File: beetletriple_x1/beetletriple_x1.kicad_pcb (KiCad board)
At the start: 4 copper layers, 82 x 56.5 mm, 70 parts, among them J1 Power IN, J10 soicbite programming connector, J2 motor_out, J3 motor_out, J4 motor_out, J5 input_c1, J6 input_c2, J7 input_c3, J8 output_c4, J9 output_c5, Q1 IRF8313PBF, Q2 IRF8313PBF, Q3 IRF8313PBF, Q4 IRF8313PBF, Q5 IRF8313PBF, Q6 IRF8313PBF, U1 TPS54331DR, U11 NCP81155MN, U12 NCP81155MN, U13 NCP81155MN, U14 NCP81155MN, U15 NCP81155MN, U16 NCP81155MN, U2 HT7550-1, U3 ATtiny1617-M, U4 78L12G-AB3-R

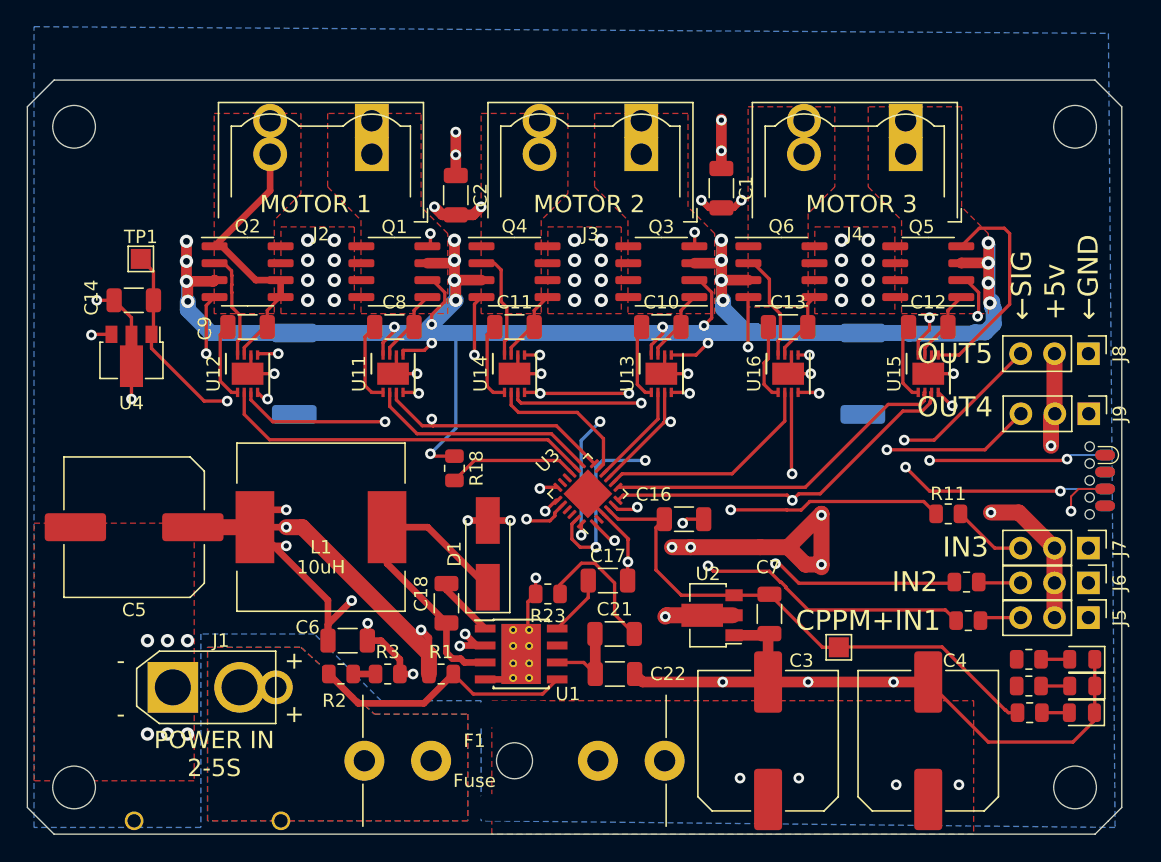
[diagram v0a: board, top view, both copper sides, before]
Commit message: Beetletriple version x1 with the dfn-8 gate driver finally fix up routing and errors
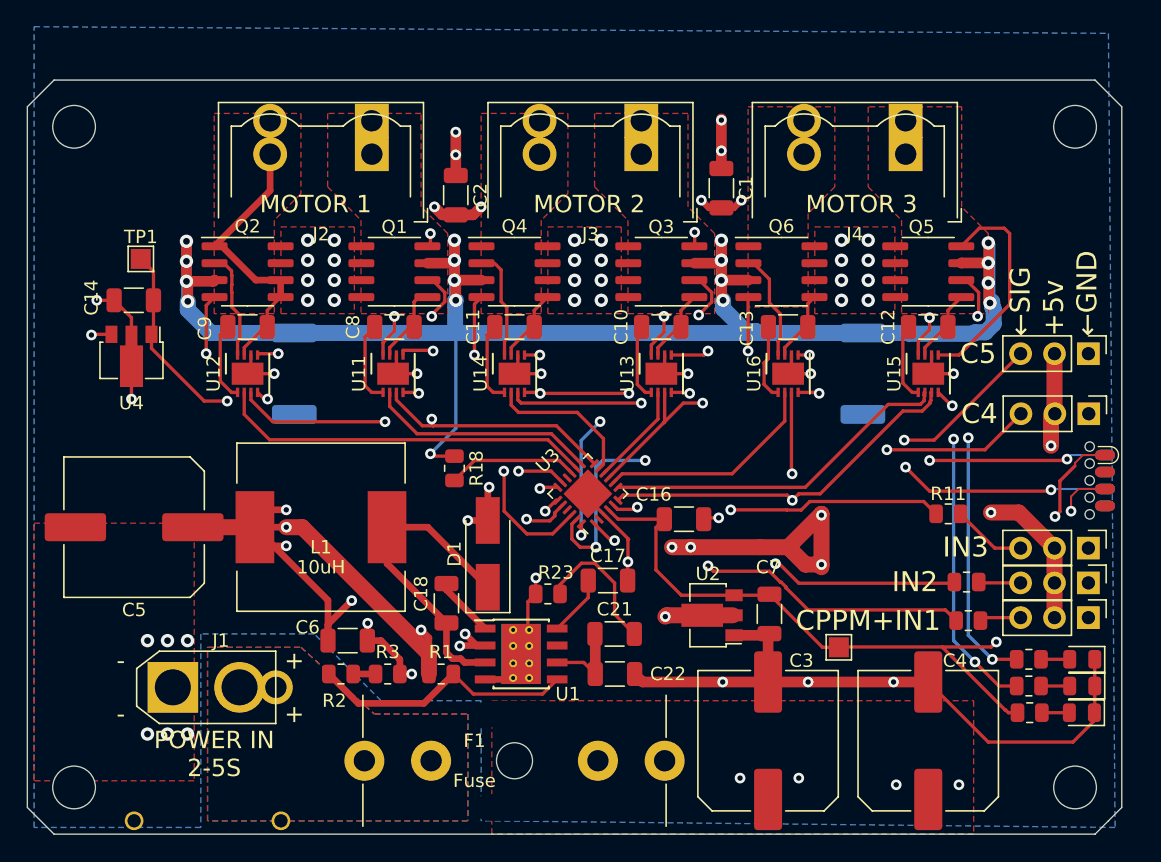
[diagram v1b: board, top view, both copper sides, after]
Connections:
- U3 pad 17: unconnected-(U3-Pad17) -> /MCU/BLINKY2
- U3 pad 21: /MCU/BLINKY2 -> unconnected-(U3-Pad21)
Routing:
- net /MCU/BLINKY1: track 0.00 -> 66.4 mm, vias 0 -> 3
- net /MCU/BLINKY2: track 0.00 -> 60.5 mm, vias 0 -> 3
- net VLOGIC: track 40.7 -> 64.4 mm, vias 0 -> 2
- net MOTOR2EN: track 21.4 -> 26.2 mm
- net /Drivers/GNDSHUNT: track 145.9 -> 144.9 mm
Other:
- board text added: "C4"
- board text added: "C5"
- board text removed: "OUT4"
- board text removed: "OUT5"

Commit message: Add gate resistors; re-layout
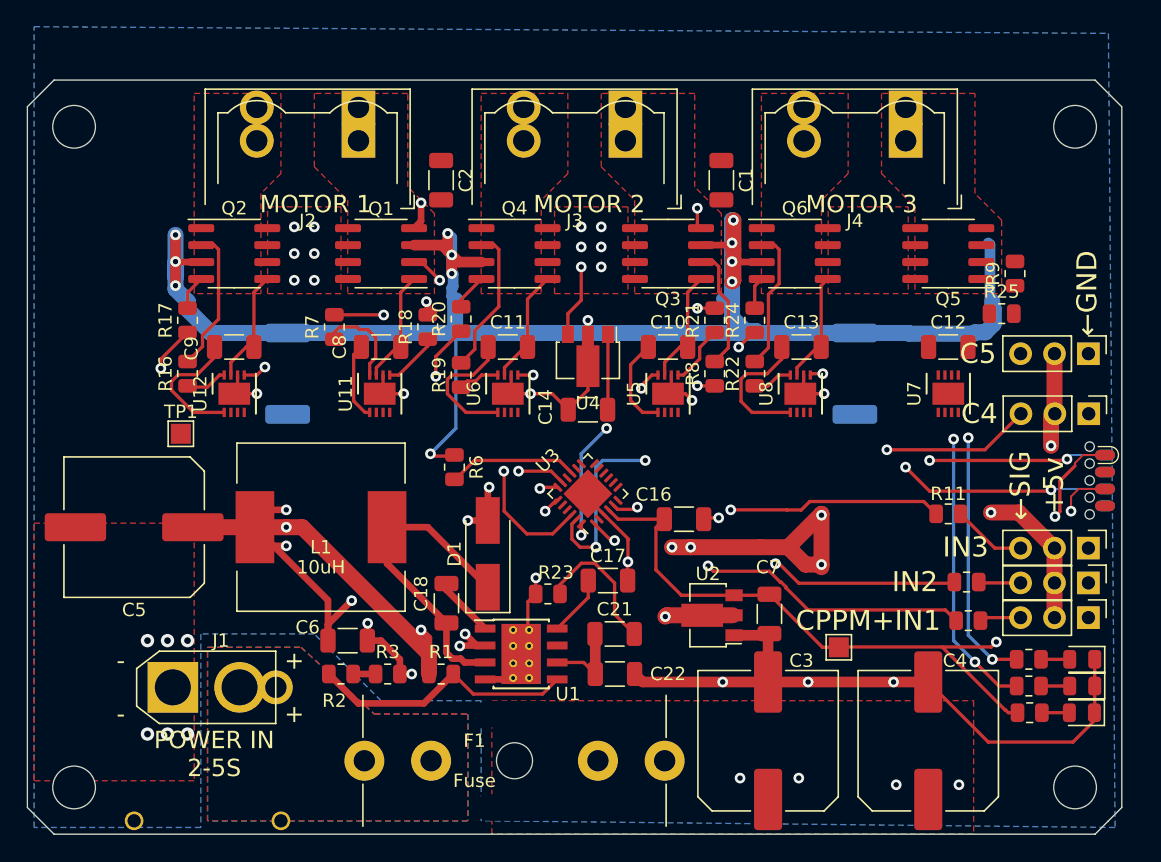
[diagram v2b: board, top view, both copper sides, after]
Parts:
- removed U13, U14, U15, U16: NCP81155MN, Package_DFN_QFN:DFN-8-1EP_3x3mm_P0.5mm_EP1.66x2.38mm
- added R19: 10R, Resistor_SMD:R_0805_2012Metric, F.Cu at (128.5, 102.6)
- added R20: 10R, Resistor_SMD:R_0805_2012Metric, F.Cu at (128.5, 98.4)
- added R21: 10R, Resistor_SMD:R_0805_2012Metric, F.Cu at (147.5, 98.5)
- added R22: 10R, Resistor_SMD:R_0805_2012Metric, F.Cu at (150.5, 102.5)
- added R24: 10R, Resistor_SMD:R_0805_2012Metric, F.Cu at (150.5, 98.5)
- added R25: 10R, Resistor_SMD:R_0805_2012Metric, F.Cu at (169.0, 98.0)
- added R4: 0.01R shunt, Resistor_SMD:R_2512_6332Metric_Pad1.40x3.35mm_HandSolder, B.Cu at (158.0, 102.5)
- added R5: 0.01R shunt, Resistor_SMD:R_2512_6332Metric_Pad1.40x3.35mm_HandSolder, B.Cu at (115.5, 102.5)
- added R6: 1.5k, Resistor_SMD:R_0805_2012Metric, F.Cu at (128.0, 109.5)
- added R7: 10R, Resistor_SMD:R_0805_2012Metric, F.Cu at (119.0, 99.0)
- added R8: 10R, Resistor_SMD:R_0805_2012Metric, F.Cu at (147.5, 102.5)
- added R9: 10R, Resistor_SMD:R_0805_2012Metric, F.Cu at (170.0, 95.0)
- added U5: NCP81155MN, Package_DFN_QFN:DFN-8-1EP_3x3mm_P0.5mm_EP1.66x2.38mm, F.Cu at (144.0, 104.0)
- added U6: NCP81155MN, Package_DFN_QFN:DFN-8-1EP_3x3mm_P0.5mm_EP1.66x2.38mm, F.Cu at (132.0, 104.0)
- added U7: NCP81155MN, Package_DFN_QFN:DFN-8-1EP_3x3mm_P0.5mm_EP1.66x2.38mm, F.Cu at (165.0, 104.0)
- added U8: NCP81155MN, Package_DFN_QFN:DFN-8-1EP_3x3mm_P0.5mm_EP1.66x2.38mm, F.Cu at (153.9, 104.0)
- R16, R17: value 0.01R shunt -> 10R; footprint Resistor_SMD:R_2512_6332Metric_Pad1.40x3.35mm_HandSolder -> Resistor_SMD:R_0805_2012Metric; moved to F.Cu
- R18: value 1.5k -> 10R
- moved R16 50.6 mm to (108.0, 102.5)
- moved C14 35.0 mm to (138.0, 105.2)
- moved U4 34.2 mm to (138.0, 101.2)
- moved TP1 13.4 mm to (107.5, 107.0)
- moved R18 10.8 mm to (126.0, 99.0), turned to 90 degrees
- moved R17 8.94 mm to (108.0, 98.5)
- moved C12 2.12 mm to (165.0, 100.5)
- moved Q5 2.02 mm to (165.0, 93.5)
- moved C13 1.80 mm to (154.0, 100.5)
- moved C8 1.80 mm to (122.5, 100.5)
- moved C9 1.80 mm to (111.5, 100.5)
- moved U11 1.80 mm to (122.4, 104.0)
- moved U12 1.80 mm to (111.5, 104.0)
- moved Q1 1.68 mm to (122.5, 93.5)
- moved Q2 1.68 mm to (111.5, 93.5)
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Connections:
- net /Drivers/M1S1 renamed /driver1/MOTORS1
- net /Drivers/M1S2 renamed /driver1/MOTORS2
- net /Drivers/M2S1 renamed /driver2/MOTORS1
- net /Drivers/M2S2 renamed /driver2/MOTORS2
- net /Drivers/M3S1 renamed /driver3/MOTORS1
- net /Drivers/M3S2 renamed /driver3/MOTORS2
- Q1 pad 2: /Drivers/M1H1 -> /driver1/GATEH1
- Q1 pad 3: /Drivers/GNDSHUNT -> GNDSHUNT
- Q1 pad 4: /Drivers/M1L1 -> /driver1/GATEL1
- Q2 pad 2: /Drivers/M1H2 -> /driver1/GATEH2
- Q2 pad 3: /Drivers/GNDSHUNT -> GNDSHUNT
- Q2 pad 4: /Drivers/M1L2 -> /driver1/GATEL2
- Q3 pad 2: /Drivers/M2H1 -> /driver2/GATEH1
- Q3 pad 3: /Drivers/GNDSHUNT -> GNDSHUNT
- Q3 pad 4: /Drivers/M2L1 -> /driver2/GATEL1
- Q4 pad 2: /Drivers/M2H2 -> /driver2/GATEH2
- Q4 pad 3: /Drivers/GNDSHUNT -> GNDSHUNT
- Q4 pad 4: /Drivers/M2L2 -> /driver2/GATEL2
- Q5 pad 2: /Drivers/M3H1 -> /driver3/GATEH1
- Q5 pad 3: /Drivers/GNDSHUNT -> GNDSHUNT
- Q5 pad 4: /Drivers/M3L1 -> /driver3/GATEL1
- Q6 pad 2: /Drivers/M3H2 -> /driver3/GATEH2
- Q6 pad 3: /Drivers/GNDSHUNT -> GNDSHUNT
- Q6 pad 4: /Drivers/M3L2 -> /driver3/GATEL2
- R16 pad 1: GND -> /driver1/MOTORH2
- R16 pad 2: /Drivers/GNDSHUNT -> /driver1/GATEH2
- R17 pad 1: GND -> /driver1/MOTORL2
- R17 pad 2: /Drivers/GNDSHUNT -> /driver1/GATEL2
- R18 pad 1: /Drivers/GNDSHUNT -> /driver1/MOTORL1
- R18 pad 2: CURRENTSENSE -> /driver1/GATEL1
- U11 pad 5: /Drivers/M1L1 -> /driver1/MOTORL1
- U11 pad 8: /Drivers/M1H1 -> /driver1/MOTORH1
- U12 pad 5: /Drivers/M1L2 -> /driver1/MOTORL2
- U12 pad 8: /Drivers/M1H2 -> /driver1/MOTORH2
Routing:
- net /Drivers/GNDSHUNT: track 144.9 -> 0.00 mm, vias 17 -> 0
- net GNDSHUNT: track 0.00 -> 142.8 mm, vias 0 -> 11
- net +12V: track 77.3 -> 5.66 mm, vias 8 -> 0
- net /MCU/SERVO1: track 47.6 -> 0.00 mm, vias 2 -> 0
- net MOTOR3EN: track 35.7 -> 0.00 mm, vias 2 -> 0
- net MOTOR1EN: track 32.8 -> 0.00 mm, vias 2 -> 0
- net MOTOR1D2: track 28.2 -> 0.00 mm
- net MOTOR3D1: track 26.3 -> 0.00 mm
- net MOTOR2EN: track 26.2 -> 0.00 mm, vias 2 -> 0
- net MOTOR1D1: track 17.2 -> 0.00 mm
- net MOTOR3D2: track 16.9 -> 0.00 mm
- net /Drivers/M3L1: track 16.6 -> 0.00 mm
- net /Drivers/M2L1: track 13.6 -> 0.00 mm, vias 2 -> 0
- net /driver1/MOTORL2: track 0.00 -> 13.2 mm, vias 0 -> 2
- net /Drivers/M1L1: track 13.1 -> 0.00 mm, vias 2 -> 0
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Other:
- board text added: "BBB receiver"

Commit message: Footprints shenanigans
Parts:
- added TP3: TestPoint, TestPoint:TestPoint_Pad_1.5x1.5mm, F.Cu at (102.9, 92.1)
- added TP4: TestPoint, TestPoint:TestPoint_Pad_1.5x1.5mm, F.Cu at (102.9, 95.7)
- U11, U12, U5, U6, U7, U8: footprint Package_DFN_QFN:DFN-8-1EP_3x3mm_P0.5mm_EP1.66x2.38mm -> beetletriple:DFN-8-3x3mm_hand1
- U3: footprint Package_DFN_QFN:QFN-24-1EP_4x4mm_P0.5mm_EP2.6x2.6mm -> beetletriple:qfn24-hand1
- moved TP1 9.61 mm to (116.6, 103.9)
- moved C2 1.12 mm to (127.2, 86.9)
- moved C1 1.10 mm to (148.0, 86.9)
- moved C8 0.30 mm to (122.5, 100.2)
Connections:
- U3 pad 18: /MCU/RXIN2 -> /MCU/SERVO2
- U3 pad 19: /MCU/SERVO2 -> /MCU/RXIN2
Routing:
- net +12V: track 5.66 -> 79.8 mm, vias 0 -> 7
- net /MCU/SERVO1: track 0.00 -> 51.4 mm, vias 0 -> 2
- net MOTOR3EN: track 0.00 -> 36.9 mm, vias 0 -> 2
- net MOTOR1EN: track 0.00 -> 33.9 mm, vias 0 -> 2
- net MOTOR1D2: track 0.00 -> 28.3 mm
- net MOTOR3D1: track 0.00 -> 27.2 mm
- net /driver1/GATEL1: track 10.7 -> 35.5 mm, vias 2 -> 3
- net MOTOR2EN: track 0.00 -> 24.7 mm, vias 0 -> 2
- net MOTOR1D1: track 0.00 -> 17.6 mm
- net /driver1/GATEH1: track 12.5 -> 29.6 mm, vias 2 -> 4
- net MOTOR3D2: track 0.00 -> 16.5 mm
- net /driver3/MOTORH1: track 0.00 -> 13.5 mm, vias 0 -> 2
- net /driver3/GATEL1: track 0.00 -> 11.7 mm
- net MOTOR2D2: track 0.00 -> 10.9 mm
- net /driver3/MOTORS1: track 0.00 -> 8.72 mm
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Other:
- board text added: "←SIG→"
- board text removed: "C4"
- board text removed: "C5"
- board text removed: "←SIG"

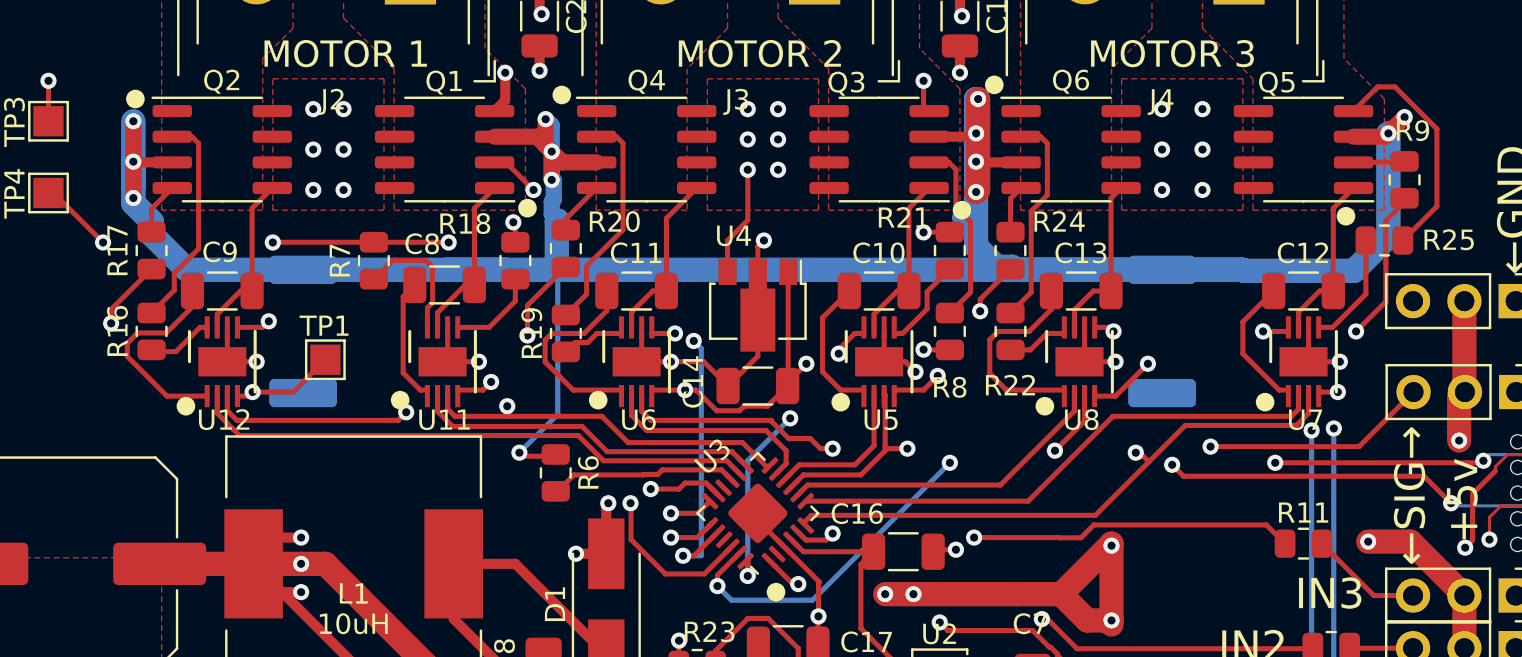
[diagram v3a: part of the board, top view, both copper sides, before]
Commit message: Add another capacitor on 12v line
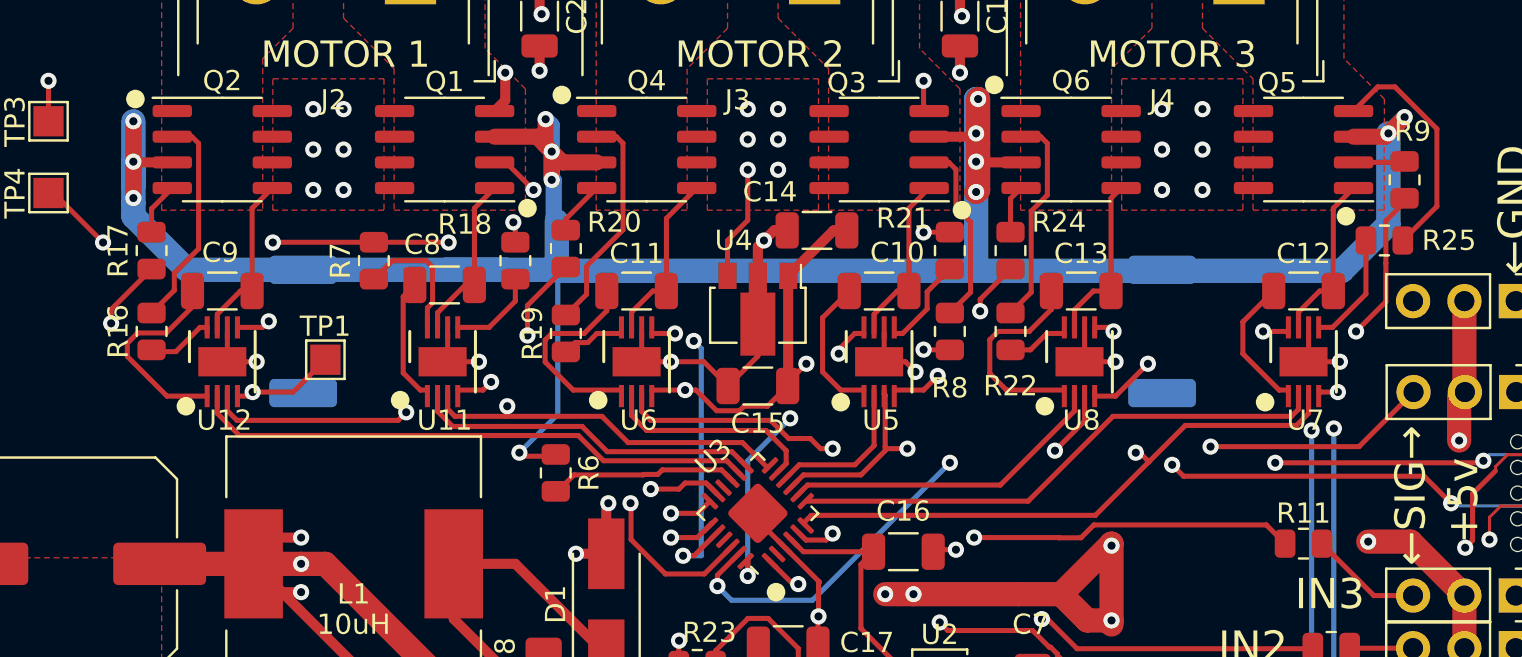
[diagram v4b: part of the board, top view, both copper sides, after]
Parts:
- added C15: 10uF 50V, Capacitor_SMD:C_1206_3216Metric, F.Cu at (138.0, 105.2)
- U11, U12, U5, U6, U7, U8: value NCP81155MN -> NCP81155MNTXG
- moved C14 8.24 mm to (140.9, 97.5)
- moved U4 0.20 mm to (138.0, 101.4)
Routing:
- net GNDSHUNT: track 146.9 -> 133.4 mm
- net +12V: track 79.8 -> 83.4 mm
- net GND: track 111.3 -> 112.7 mm

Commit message: minor updates
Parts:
- F1: footprint beetletriple:fuseholder_flexible -> beetletriple:fuseholder_bs1363
- moved F1 3.25 mm to (118.0, 131.6)
- moved J1 0.78 mm to (106.4, 125.5)
